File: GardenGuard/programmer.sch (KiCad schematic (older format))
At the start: 28 parts

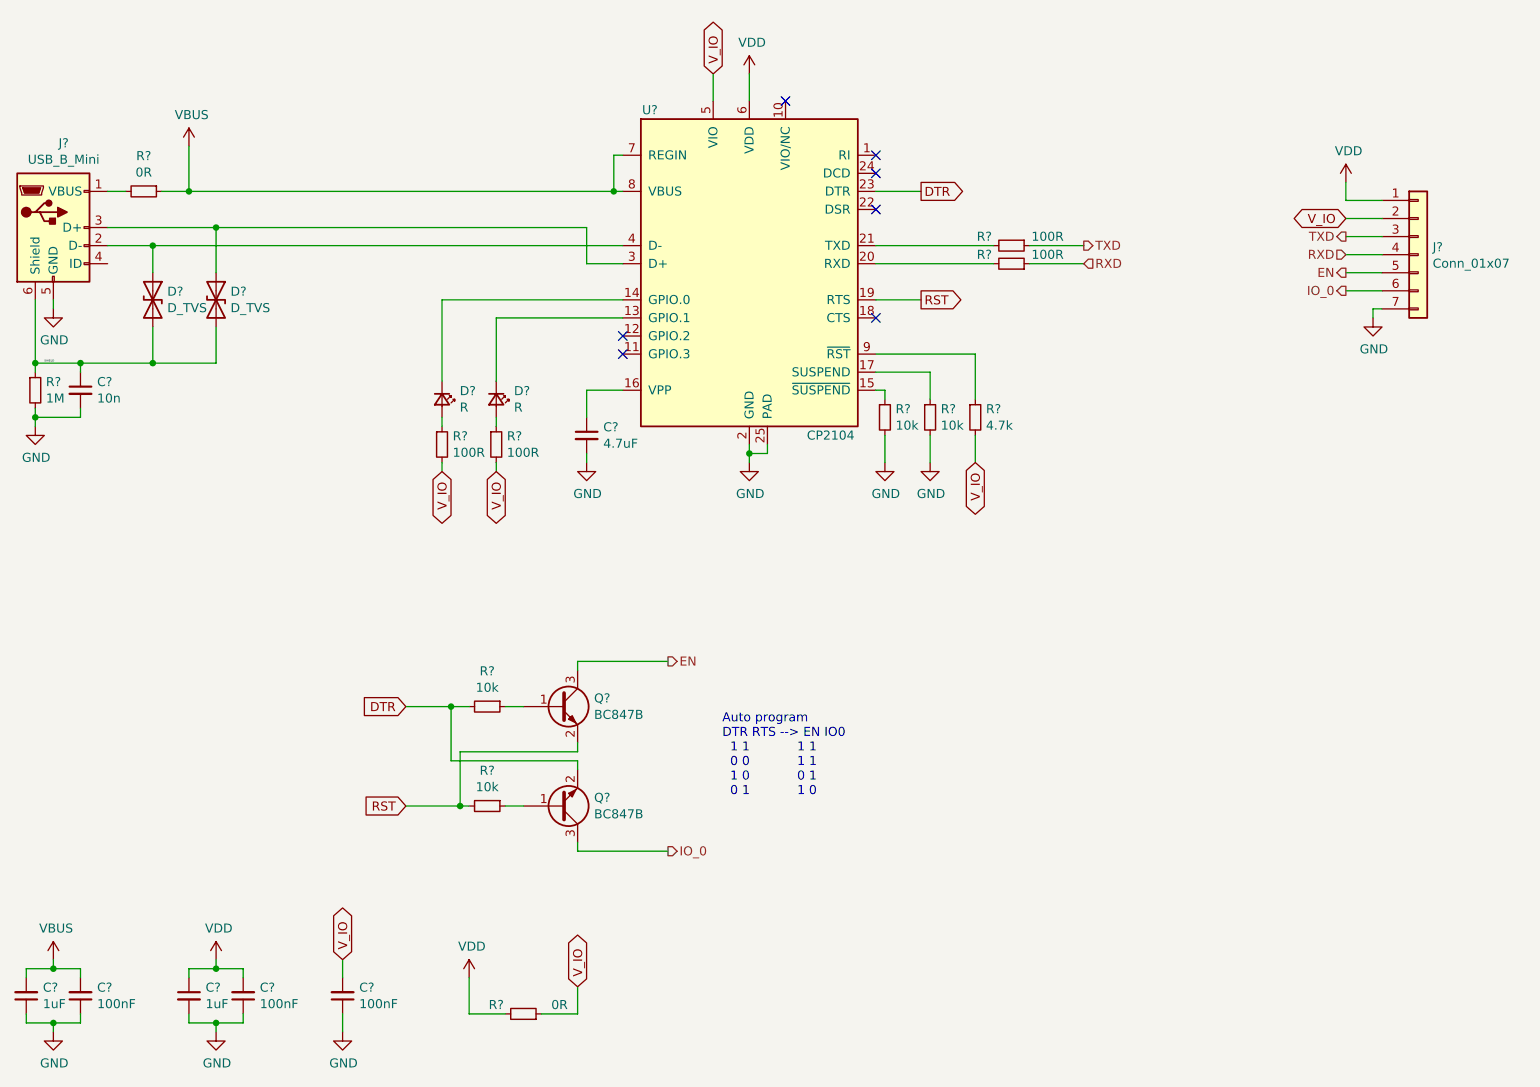
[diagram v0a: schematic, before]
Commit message: Added powersupply stages
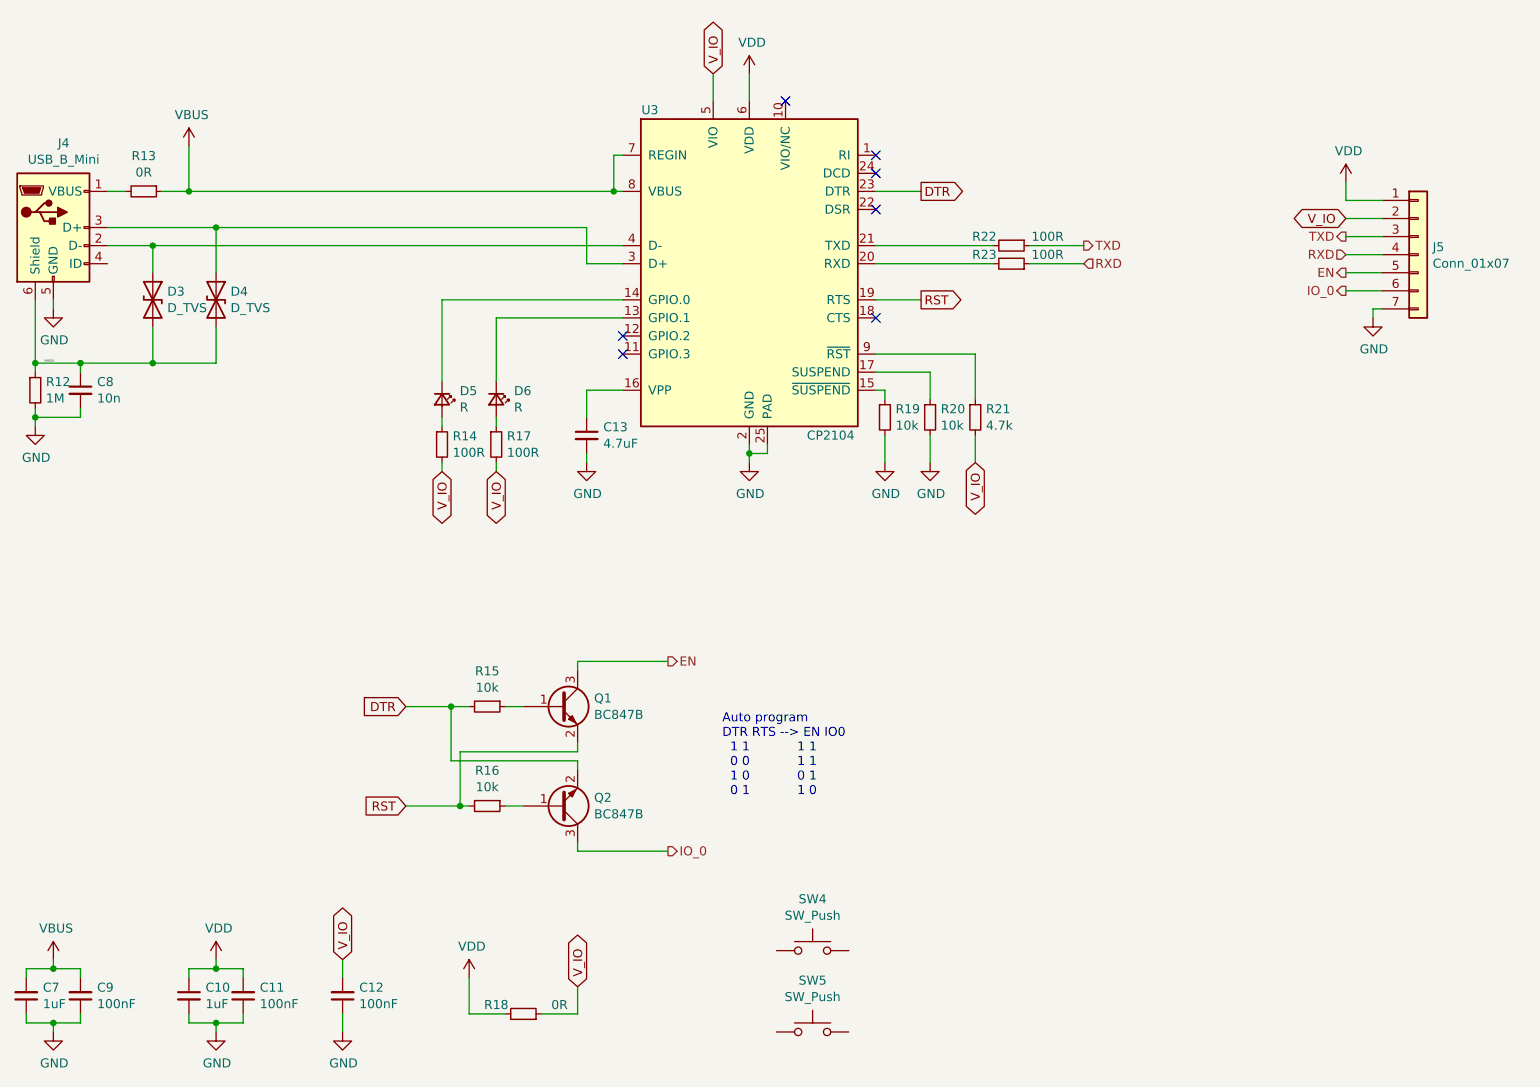
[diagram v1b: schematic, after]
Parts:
- added SW4, SW5: SW_Push, Button_Switch_SMD:SW_SPST_B3U-3000P, symbol Switch:SW_Push
- C10, C11, C12, C13, C7, C8, C9: renamed from C?; footprint (none) -> Capacitor_SMD:C_0805_2012Metric_Pad1.18x1.45mm_HandSolder
- D3, D4: renamed from D?; footprint (none) -> Diode_SMD:D_0805_2012Metric_Castellated
- D5, D6: renamed from D?; footprint (none) -> LED_SMD:LED_0805_2012Metric_Pad1.15x1.40mm_HandSolder
- J4: renamed from J?; footprint (none) -> Connector_USB:USB_Micro-B_Amphenol_10118194_Horizontal
- J5: renamed from J?; footprint (none) -> Connector_PinHeader_2.54mm:PinHeader_1x07_P2.54mm_Vertical
- Q1, Q2: renamed from Q?; footprint (none) -> Package_TO_SOT_SMD:SOT-23
- R12, R13, R14, R15, R16, R17, R18, R19, R20, R21, R22, R23: renamed from R?; footprint (none) -> Resistor_SMD:R_0805_2012Metric_Pad1.20x1.40mm_HandSolder
- gave numbers to parts that had none: 1
